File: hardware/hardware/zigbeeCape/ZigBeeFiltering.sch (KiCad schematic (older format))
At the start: 27 parts, among them U2 0.8Ghz_and_2.4GHz_Filter, U3 SMA_Antenna

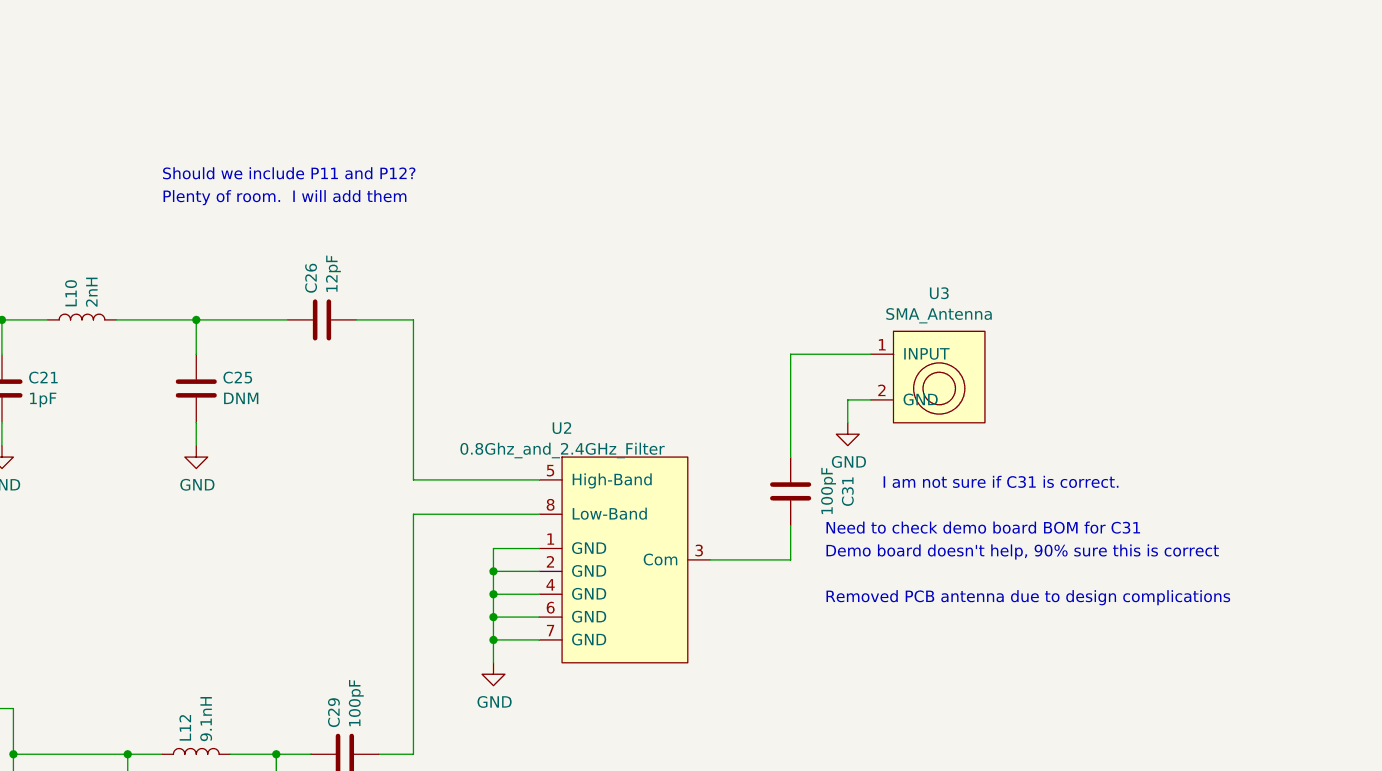
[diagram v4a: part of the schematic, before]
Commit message: Added Schematic pdf
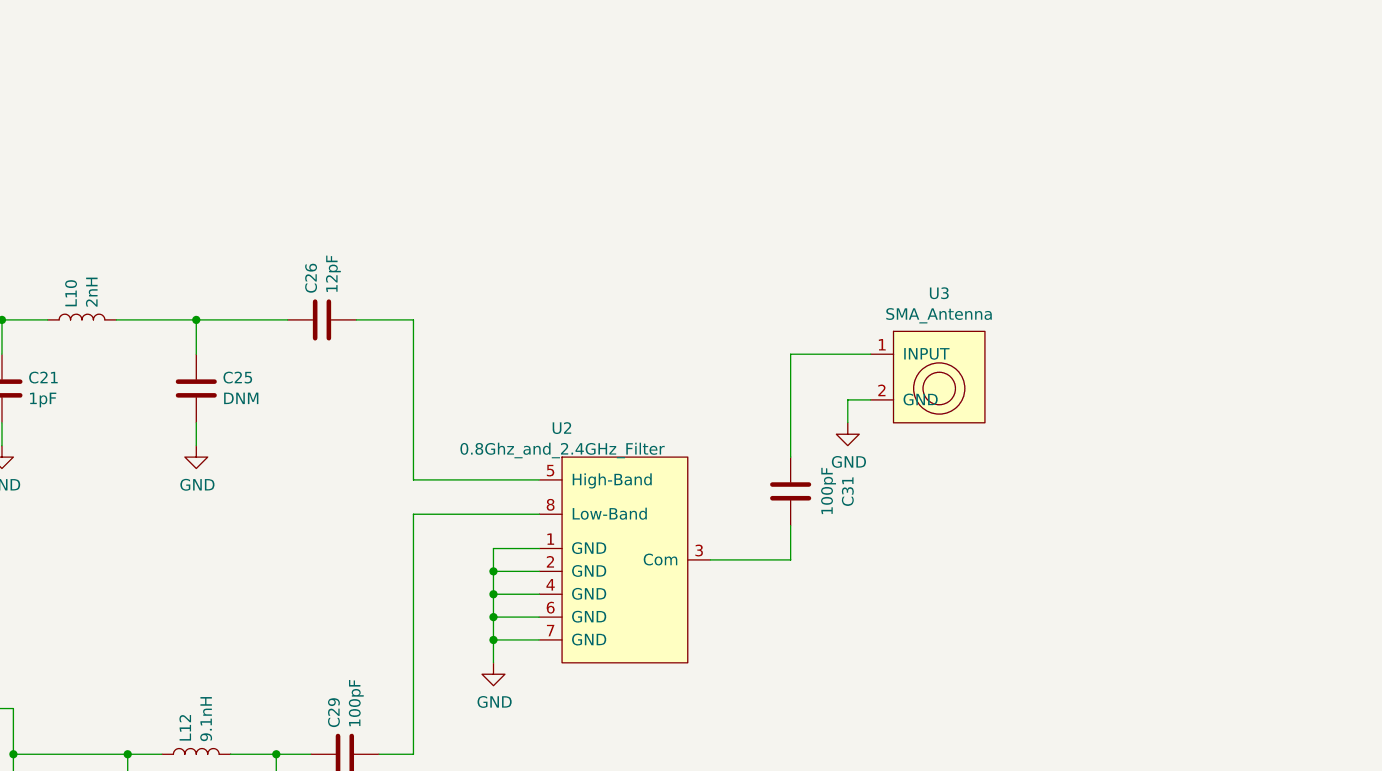
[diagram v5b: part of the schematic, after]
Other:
- note removed: "Demo board doesn't help, 90% sure this is correct"
- note removed: "I am not sure if C31 is correct."
- note removed: "Need to check demo board BOM for C31"
- note removed: "Plenty of room. I will add them"
- note removed: "Removed PCB antenna due to design complications"
- note removed: "Should we include P11 and P12?"
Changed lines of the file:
@@
 Wire Wire Line
 	7150 4100 7150 4250
-Text Notes 4400 2600 0    50   ~ 0
-Should we include P11 and P12?
 Text HLabel 2150 3000 0    50   Input ~ 0
 2_4_GHZ_RF_P
@@
 	-1   0    0    1
 $EndComp
-Text Notes 7550 3950 0    50   ~ 0
-I am not sure if C31 is correct.
-Text Notes 7300 4450 0    50   ~ 0
-Removed PCB antenna due to design complications
-Text Notes 7300 4150 0    50   ~ 0
-Need to check demo board BOM for C31
-Text Notes 7300 4250 0    50   ~ 0
-Demo board doesn't help, 90% sure this is correct
-Text Notes 4400 2700 0    50   ~ 0
-Plenty of room.  I will add them
 $EndSCHEMATC

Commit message: Rerouted main ZigBee Lines
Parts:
- C17, C18, C19, C20, C21, C22, C23, C24, C25, C26, C27, C28, C29, C31: footprint Capacitor_SMD:C_0603_1608Metric_Pad1.08x0.95mm_HandSolder -> Capacitor_SMD:C_0402_1005Metric_Pad0.74x0.62mm_HandSolder
- L11, L12, L5, L6, L8, L9: footprint Inductor_SMD:L_0603_1608Metric_Pad1.05x0.95mm_HandSolder -> Inductor_SMD:L_0402_1005Metric_Pad0.77x0.64mm_HandSolder
- L2: footprint Inductor_SMD:L_0805_2012Metric_Pad1.15x1.40mm_HandSolder -> Inductor_SMD:L_0402_1005Metric_Pad0.77x0.64mm_HandSolder
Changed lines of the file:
@@
 F 0 "C24" H 3515 4946 50  0000 L CNN
 F 1 "3pF" H 3515 4855 50  0000 L CNN
-F 2 "Capacitor_SMD:C_0603_1608Metric_Pad1.08x0.95mm_HandSolder" H 3438 4750 50  0001 C CNN
+F 2 "Capacitor_SMD:C_0402_1005Metric_Pad0.74x0.62mm_HandSolder" H 3438 4750 50  0001 C CNN
 F 3 "~" H 3400 4900 50  0001 C CNN
 	1    3400 4900
@@
 F 0 "L5" H 2253 4946 50  0000 L CNN
 F 1 "3.9nH" H 2253 4855 50  0000 L CNN
-F 2 "Inductor_SMD:L_0603_1608Metric_Pad1.05x0.95mm_HandSolder" H 2200 4900 50  0001 C CNN
+F 2 "Inductor_SMD:L_0402_1005Metric_Pad0.77x0.64mm_HandSolder" H 2200 4900 50  0001 C CNN
 F 3 "~" H 2200 4900 50  0001 C CNN
 	1    2200 4900
@@
 F 0 "C22" H 3115 4296 50  0000 L CNN
 F 1 "100pF" H 3115 4205 50  0000 L CNN
-F 2 "Capacitor_SMD:C_0603_1608Metric_Pad1.08x0.95mm_HandSolder" H 3038 4100 50  0001 C CNN
+F 2 "Capacitor_SMD:C_0402_1005Metric_Pad0.74x0.62mm_HandSolder" H 3038 4100 50  0001 C CNN
 F 3 "~" H 3000 4250 50  0001 C CNN
 	1    3000 4250
@@
 F 0 "L6" H 2253 5346 50  0000 L CNN
 F 1 "3.9nH" H 2253 5255 50  0000 L CNN
-F 2 "Inductor_SMD:L_0603_1608Metric_Pad1.05x0.95mm_HandSolder" H 2200 5300 50  0001 C CNN
+F 2 "Inductor_SMD:L_0402_1005Metric_Pad0.77x0.64mm_HandSolder" H 2200 5300 50  0001 C CNN
 F 3 "~" H 2200 5300 50  0001 C CNN
 	1    2200 5300
@@
 F 0 "C27" H 4365 5546 50  0000 L CNN
 F 1 "DNM" H 4365 5455 50  0000 L CNN
-F 2 "Capacitor_SMD:C_0603_1608Metric_Pad1.08x0.95mm_HandSolder" H 4288 5350 50  0001 C CNN
+F 2 "Capacitor_SMD:C_0402_1005Metric_Pad0.74x0.62mm_HandSolder" H 4288 5350 50  0001 C CNN
 F 3 "~" H 4250 5500 50  0001 C CNN
 	1    4250 5500
@@
 F 0 "L9" H 3053 4696 50  0000 L CNN
 F 1 "10nH" H 3053 4605 50  0000 L CNN
-F 2 "Inductor_SMD:L_0603_1608Metric_Pad1.05x0.95mm_HandSolder" H 3000 4650 50  0001 C CNN
+F 2 "Inductor_SMD:L_0402_1005Metric_Pad0.77x0.64mm_HandSolder" H 3000 4650 50  0001 C CNN
 F 3 "~" H 3000 4650 50  0001 C CNN
 	1    3000 4650
@@
 F 0 "C28" H 5015 5546 50  0000 L CNN
 F 1 "3.6pF" H 5015 5455 50  0000 L CNN
-F 2 "Capacitor_SMD:C_0603_1608Metric_Pad1.08x0.95mm_HandSolder" H 4938 5350 50  0001 C CNN
+F 2 "Capacitor_SMD:C_0402_1005Metric_Pad0.74x0.62mm_HandSolder" H 4938 5350 50  0001 C CNN
 F 3 "~" H 4900 5500 50  0001 C CNN
 	1    4900 5500
@@
 F 0 "L12" H 4603 5146 50  0000 L CNN
 F 1 "9.1nH" H 4603 5055 50  0000 L CNN
-F 2 "Inductor_SMD:L_0603_1608Metric_Pad1.05x0.95mm_HandSolder" H 4550 5100 50  0001 C CNN
+F 2 "Inductor_SMD:L_0402_1005Metric_Pad0.77x0.64mm_HandSolder" H 4550 5100 50  0001 C CNN
 F 3 "~" H 4550 5100 50  0001 C CNN
 	1    4550 5100
@@
 F 0 "C29" H 5315 5146 50  0000 L CNN
 F 1 "100pF" H 5315 5055 50  0000 L CNN
-F 2 "Capacitor_SMD:C_0603_1608Metric_Pad1.08x0.95mm_HandSolder" H 5238 4950 50  0001 C CNN
+F 2 "Capacitor_SMD:C_0402_1005Metric_Pad0.74x0.62mm_HandSolder" H 5238 4950 50  0001 C CNN
 F 3 "~" H 5200 5100 50  0001 C CNN
 	1    5200 5100
@@
 F 0 "C23" H 3215 5546 50  0000 L CNN
 F 1 "3pF" H 3215 5455 50  0000 L CNN
-F 2 "Capacitor_SMD:C_0603_1608Metric_Pad1.08x0.95mm_HandSolder" H 3138 5350 50  0001 C CNN
+F 2 "Capacitor_SMD:C_0402_1005Metric_Pad0.74x0.62mm_HandSolder" H 3138 5350 50  0001 C CNN
 F 3 "~" H 3100 5500 50  0001 C CNN
 	1    3100 5500
@@
 F 0 "L11" H 3453 5346 50  0000 L CNN
 F 1 "10nH" H 3453 5255 50  0000 L CNN
-F 2 "Inductor_SMD:L_0603_1608Metric_Pad1.05x0.95mm_HandSolder" H 3400 5300 50  0001 C CNN
+F 2 "Inductor_SMD:L_0402_1005Metric_Pad0.77x0.64mm_HandSolder" H 3400 5300 50  0001 C CNN
 F 3 "~" H 3400 5300 50  0001 C CNN
 	1    3400 5300
@@
 F 0 "C20" H 2615 5146 50  0000 L CNN
 F 1 "1.2pF" H 2615 5055 50  0000 L CNN
-F 2 "Capacitor_SMD:C_0603_1608Metric_Pad1.08x0.95mm_HandSolder" H 2538 4950 50  0001 C CNN
+F 2 "Capacitor_SMD:C_0402_1005Metric_Pad0.74x0.62mm_HandSolder" H 2538 4950 50  0001 C CNN
 F 3 "~" H 2500 5100 50  0001 C CNN
 	1    2500 5100
@@
 F 0 "L8" H 2903 5146 50  0000 L CNN
 F 1 "22nH" H 2903 5055 50  0000 L CNN
-F 2 "Inductor_SMD:L_0603_1608Metric_Pad1.05x0.95mm_HandSolder" H 2850 5100 50  0001 C CNN
+F 2 "Inductor_SMD:L_0402_1005Metric_Pad0.77x0.64mm_HandSolder" H 2850 5100 50  0001 C CNN
 F 3 "~" H 2850 5100 50  0001 C CNN
 	1    2850 5100
@@
 F 0 "C19" H 2965 3046 50  0000 L CNN
 F 1 "1.1pF" H 2965 2955 50  0000 L CNN
-F 2 "Capacitor_SMD:C_0603_1608Metric_Pad1.08x0.95mm_HandSolder" H 2888 2850 50  0001 C CNN
+F 2 "Capacitor_SMD:C_0402_1005Metric_Pad0.74x0.62mm_HandSolder" H 2888 2850 50  0001 C CNN
 F 3 "~" H 2850 3000 50  0001 C CNN
 	1    2850 3000
@@
 F 0 "C26" H 5215 3246 50  0000 L CNN
 F 1 "12pF" H 5215 3155 50  0000 L CNN
-F 2 "Capacitor_SMD:C_0603_1608Metric_Pad1.08x0.95mm_HandSolder" H 5138 3050 50  0001 C CNN
+F 2 "Capacitor_SMD:C_0402_1005Metric_Pad0.74x0.62mm_HandSolder" H 5138 3050 50  0001 C CNN
 F 3 "~" H 5100 3200 50  0001 C CNN
 	1    5100 3200
@@
 F 0 "C25" H 4665 3546 50  0000 L CNN
 F 1 "DNM" H 4665 3455 50  0000 L CNN
-F 2 "Capacitor_SMD:C_0603_1608Metric_Pad1.08x0.95mm_HandSolder" H 4588 3350 50  0001 C CNN
+F 2 "Capacitor_SMD:C_0402_1005Metric_Pad0.74x0.62mm_HandSolder" H 4588 3350 50  0001 C CNN
 F 3 "~" H 4550 3500 50  0001 C CNN
 	1    4550 3500
@@
 F 0 "C21" H 3815 3546 50  0000 L CNN
 F 1 "1pF" H 3815 3455 50  0000 L CNN
-F 2 "Capacitor_SMD:C_0603_1608Metric_Pad1.08x0.95mm_HandSolder" H 3738 3350 50  0001 C CNN
+F 2 "Capacitor_SMD:C_0402_1005Metric_Pad0.74x0.62mm_HandSolder" H 3738 3350 50  0001 C CNN
 F 3 "~" H 3700 3500 50  0001 C CNN
 	1    3700 3500
@@
 F 0 "C17" H 2615 2346 50  0000 L CNN
 F 1 "12pF" H 2615 2255 50  0000 L CNN
-F 2 "Capacitor_SMD:C_0603_1608Metric_Pad1.08x0.95mm_HandSolder" H 2538 2150 50  0001 C CNN
+F 2 "Capacitor_SMD:C_0402_1005Metric_Pad0.74x0.62mm_HandSolder" H 2538 2150 50  0001 C CNN
 F 3 "~" H 2500 2300 50  0001 C CNN
 	1    2500 2300
@@
 F 0 "C18" H 2615 3796 50  0000 L CNN
 F 1 "1.1pF" H 2615 3705 50  0000 L CNN
-F 2 "Capacitor_SMD:C_0603_1608Metric_Pad1.08x0.95mm_HandSolder" H 2538 3600 50  0001 C CNN
+F 2 "Capacitor_SMD:C_0402_1005Metric_Pad0.74x0.62mm_HandSolder" H 2538 3600 50  0001 C CNN
 F 3 "~" H 2500 3750 50  0001 C CNN
 	1    2500 3750
@@
 F 0 "L2" H 2353 3296 50  0000 L CNN
 F 1 "15nH" H 2353 3205 50  0000 L CNN
-F 2 "Inductor_SMD:L_0805_2012Metric_Pad1.15x1.40mm_HandSolder" H 2300 3250 50  0001 C CNN
+F 2 "Inductor_SMD:L_0402_1005Metric_Pad0.77x0.64mm_HandSolder" H 2300 3250 50  0001 C CNN
 F 3 "~" H 2300 3250 50  0001 C CNN
 	1    2300 3250
@@
 F 0 "C31" V 6898 3950 50  0000 C CNN
 F 1 "100pF" V 6989 3950 50  0000 C CNN
-F 2 "Capacitor_SMD:C_0603_1608Metric_Pad1.08x0.95mm_HandSolder" H 7188 3800 50  0001 C CNN
+F 2 "Capacitor_SMD:C_0402_1005Metric_Pad0.74x0.62mm_HandSolder" H 7188 3800 50  0001 C CNN
 F 3 "~" H 7150 3950 50  0001 C CNN
 	1    7150 3950
